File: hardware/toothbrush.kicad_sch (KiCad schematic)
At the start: 16 parts, among them J2 ISP, J3 MOTOR, J4 BATTERY, Q1 FN337N, SW1 button, U1 ATmega328P-A

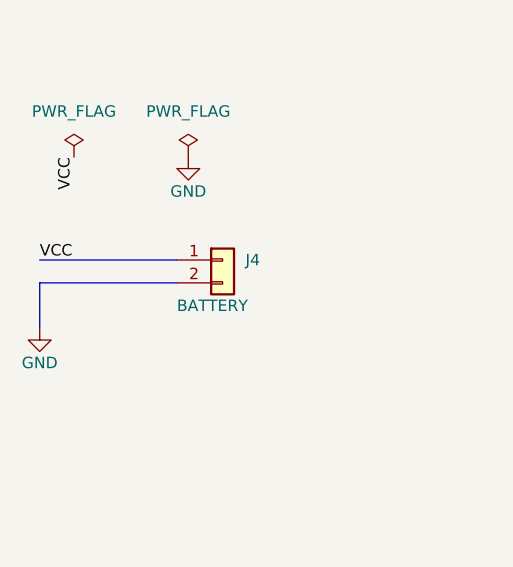
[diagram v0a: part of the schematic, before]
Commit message: Turn power connector around to be more consistent with other things.
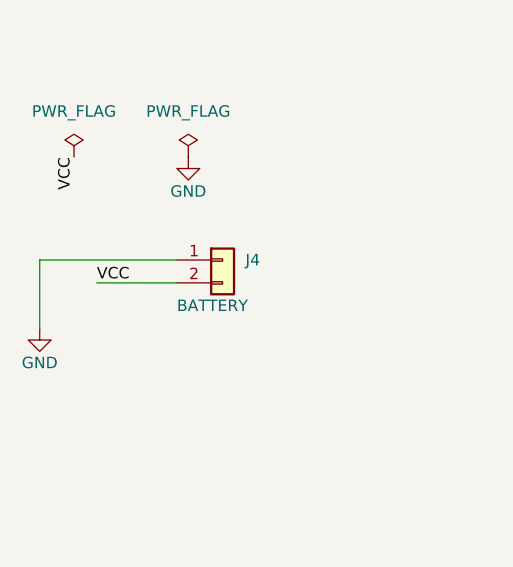
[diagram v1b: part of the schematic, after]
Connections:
- net GND: now also J4.1 (Pin_1)
- net VCC: now also J4.2 (Pin_2)
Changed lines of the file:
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@@
   (no_connect (at 156.21 133.35))
   (no_connect (at 167.64 36.83))
+  (wire (pts (xy 29.21 76.2) (xy 29.21 83.82))
+    (stroke (width 0) (type default) (color 0 0 0 0))
+  )
   (wire (pts (xy 238.76 101.6) (xy 238.76 92.71))
     (stroke (width 0) (type default) (color 0 0 0 0))
@@
     (stroke (width 0) (type default) (color 0 0 0 0))
   )
+  (wire (pts (xy 35.56 78.74) (xy 44.45 78.74))
+    (stroke (width 0) (type default) (color 0 0 0 0))
+  )
   (wire (pts (xy 156.21 82.55) (xy 175.26 82.55))
     (stroke (width 0) (type default) (color 0 0 0 0))
@@
     (stroke (width 0) (type default) (color 0 0 0 0))
   )
-  (bus (pts (xy 44.45 78.74) (xy 29.21 78.74))
-    (stroke (width 0) (type default) (color 0 0 0 0))
-  )
   (wire (pts (xy 160.02 45.72) (xy 160.02 48.26))
     (stroke (width 0) (type default) (color 0 0 0 0))
@@
     (stroke (width 0) (type default) (color 0 0 0 0))
   )
-  (bus (pts (xy 29.21 78.74) (xy 29.21 83.82))
-    (stroke (width 0) (type default) (color 0 0 0 0))
-  )
   (wire (pts (xy 208.28 123.19) (xy 217.17 123.19))
     (stroke (width 0) (type default) (color 0 0 0 0))
   )
+  (wire (pts (xy 29.21 76.2) (xy 44.45 76.2))
+    (stroke (width 0) (type default) (color 0 0 0 0))
+  )
   (wire (pts (xy 140.97 62.23) (xy 143.51 62.23))
     (stroke (width 0) (type default) (color 0 0 0 0))
@@
   )
   (wire (pts (xy 231.14 114.3) (xy 238.76 114.3))
-    (stroke (width 0) (type default) (color 0 0 0 0))
-  )
-  (bus (pts (xy 29.21 76.2) (xy 44.45 76.2))
     (stroke (width 0) (type default) (color 0 0 0 0))
   )
@@
     (effects (font (size 1.524 1.524)) (justify right bottom))
   )
-  (label "VCC" (at 29.21 76.2 0)
-    (effects (font (size 1.27 1.27)) (justify left bottom))
-  )
+  (label "VCC" (at 35.56 78.74 0)
+    (effects (font (size 1.27 1.27)) (justify left bottom))
+  )
